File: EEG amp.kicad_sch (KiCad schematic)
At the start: 40 parts, among them J1 Electrodes, J2 Power, J3 Output, J4 Status, U1 AD8232, U2 TMUX154EDGS

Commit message: Messed with schematic and(I think) finished PCB
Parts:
- removed C9: 100nF, Capacitor_SMD:C_0201_0603Metric, symbol Device:C
- removed J2: Power, Connector_PinSocket_2.54mm:PinSocket_1x03_P2.54mm_Vertical, symbol Connector:Conn_01x03_Socket
- removed R11, R12: 33k, Resistor_SMD:R_1206_3216Metric, symbol Device:R_US
- removed R16, R17: 10k ±0.1%, Resistor_SMD:R_0402_1005Metric, symbol Device:R_US
- removed R19, R20, R21: 50R, Resistor_SMD:R_0402_1005Metric, symbol Device:R_US
- removed R9: 150, Resistor_SMD:R_1206_3216Metric, symbol Device:R_US
- removed U2: TMUX154EDGS, Package_SO:VSSOP-10_3x3mm_P0.5mm, symbol Analog_Switch:TMUX154EDGS
- added J2: Power, Connector_PinSocket_2.54mm:PinSocket_1x04_P2.54mm_Vertical, symbol Connector:Conn_01x04_Socket
- added U2: TS5A3159ADBVR, Package_TO_SOT_SMD:SOT-23-6, symbol Analog_Switch:TS5A3159ADBVR
- C1, C2, C8: value 0.1uF -> ECHU1C104GX5; footprint Capacitor_SMD:C_0201_0603Metric -> Capacitor_SMD:C_1210_3225Metric
- C3: value 1nF -> CC0402JRX7R9BB102; footprint Capacitor_SMD:C_0603_1608Metric -> Capacitor_SMD:C_0402_1005Metric
- C4: value 100uF -> CA45-B6R3K107T; footprint Capacitor_SMD:C_0805_2012Metric -> Capacitor_Tantalum_SMD:CP_EIA-3528-21_Kemet-B
- C5, C6: value 10uF -> CA45-A010K106T; footprint Capacitor_SMD:C_0805_2012Metric -> Capacitor_Tantalum_SMD:CP_EIA-3216-12_Kemet-S
- C7: value 14pF -> 0402CG140J500NT; footprint Capacitor_SMD:C_0201_0603Metric -> Capacitor_SMD:C_0402_1005Metric
- D1: value Green -> XL-1608UBC-04; footprint LED_THT:LED_D5.0mm -> LED_SMD:LED_0603_1608Metric
- D2: value Yellow - 2e -> XL-1608UGC-04; footprint LED_THT:LED_D5.0mm -> LED_SMD:LED_0603_1608Metric
- D3: value Yellow - 1e -> XL-1608UGC-04; footprint LED_THT:LED_D5.0mm -> LED_SMD:LED_0603_1608Metric
- D4: value Red -> XL-2012UWC; footprint LED_THT:LED_D5.0mm -> LED_SMD:LED_0805_2012Metric
- R1, R2: value 10k ±0.1% -> ARG03BTC1002; footprint Resistor_SMD:R_0402_1005Metric -> Resistor_SMD:R_0603_1608Metric
- R10: value 33k -> 0603WAD3302T5E; footprint Resistor_SMD:R_1206_3216Metric -> Resistor_SMD:R_0603_1608Metric
- R13: value 1k -> CF1/6W-7.5KΩ±5%T52; footprint Resistor_SMD:R_1206_3216Metric -> Resistor_THT:R_Axial_DIN0207_L6.3mm_D2.5mm_P5.08mm_Vertical
- R14, R15, R18: value 10k -> 1206W4F1002T5E; footprint Resistor_SMD:R_0402_1005Metric -> Resistor_SMD:R_1206_3216Metric
- R3, R5: value 330k -> SCR0402J330K; footprint Resistor_SMD:R_1206_3216Metric -> Resistor_SMD:R_0402_1005Metric
- R4, R8: value 10 -> ARG05DTC1600; footprint Resistor_SMD:R_1206_3216Metric -> Resistor_SMD:R_0805_2012Metric
- R6: value 150 -> 0603WAD3302T5E; footprint Resistor_SMD:R_1206_3216Metric -> Resistor_SMD:R_0603_1608Metric
- R7: value 33k -> 1206W4F1002T5E
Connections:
- net +3.3V: now also C8.1, D1.2 (A), R14.2, J2.2 (Pin_2), U2.5 (V+); no longer D4.2 (A), R14.1
- net 1e: now also U2.3
- net 1o: now also R15.2; no longer R15.1
- net 2e: now also U2.1
- net Aref: now also J2.3 (Pin_3); no longer C8.1
- net GND: now also D4.1 (K), R7.1, J2.4 (Pin_4), U2.2 (GND); no longer D1.1 (K)
- net Ie: now also U2.4
- net OPAMP+1: now also R4.2; no longer R7.2
- net OPAMP-1: now also R13.2, R15.1; no longer R15.2
- net connected1: now also D4.2 (A); no longer D4.1 (K)
- net shutdown: now also D1.1 (K), R14.1; no longer D1.2 (A), R14.2
- net switch: now also R7.2, U2.6
- net at C5.1, C6.2, R10.2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: now also R6.1, R8.2; no longer R7.1
- no-connect marks 3 -> 4
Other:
- moved on the sheet: C7, D1, D4, J3, J4, R13, R18, R8

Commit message: Exported various files for OnBoard
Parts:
- renumbered C4 to C1, C1 to C4, C7 to C5, C5 to C6, C6 to C7, D4 to D1, D1 to D2, D2 to D4, J3 to J2, J2 to J3, R6 to R10, R13 to R11, R7 to R12, R14 to R13, R5 to R2, R10 to R3, R2 to R4, R3 to R5, R8 to R6, R15 to R7, R18 to R8, R4 to R9
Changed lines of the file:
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@@
 		(dnp no)
 		(fields_autoplaced yes)
-		(property "Reference" "C1"
+		(property "Reference" "C4"
 			(at 166.37 21.5899 0)
 			(effects
@@
 			(project "EEG amp"
 				(path "/828fcb53-5b19-4d8c-be04-4f1b7f282370"
-					(reference "C1")
+					(reference "C4")
 					(unit 1)
 				)
@@
 		(on_board yes)
 		(dnp no)
-		(property "Reference" "D2"
+		(property "Reference" "D4"
 			(at 228.9175 85.09 0)
 			(effects
@@
 			(project "EEG amp"
 				(path "/828fcb53-5b19-4d8c-be04-4f1b7f282370"
-					(reference "D2")
+					(reference "D4")
 					(unit 1)
 				)
@@
 		(dnp no)
 		(fields_autoplaced yes)
-		(property "Reference" "D4"
+		(property "Reference" "D1"
 			(at 249.2375 74.93 0)
 			(effects
@@
 			(project "EEG amp"
 				(path "/828fcb53-5b19-4d8c-be04-4f1b7f282370"
-					(reference "D4")
+					(reference "D1")
 					(unit 1)
 				)
@@
 		(dnp no)
 		(fields_autoplaced yes)
-		(property "Reference" "R10"
+		(property "Reference" "R3"
 			(at 153.67 106.68 90)
 			(effects
@@
 			(project "EEG amp"
 				(path "/828fcb53-5b19-4d8c-be04-4f1b7f282370"
-					(reference "R10")
+					(reference "R3")
 					(unit 1)
 				)
@@
 		(dnp no)
 		(fields_autoplaced yes)
-		(property "Reference" "R4"
+		(property "Reference" "R9"
 			(at 184.15 90.17 90)
 			(effects
@@
 			(project "EEG amp"
 				(path "/828fcb53-5b19-4d8c-be04-4f1b7f282370"
-					(reference "R4")
+					(reference "R9")
 					(unit 1)
 				)
@@
 		(dnp no)
 		(fields_autoplaced yes)
-		(property "Reference" "R13"
+		(property "Reference" "R11"
 			(at 151.13 86.3599 0)
 			(effects
@@
 			(project "EEG amp"
 				(path "/828fcb53-5b19-4d8c-be04-4f1b7f282370"
-					(reference "R13")
+					(reference "R11")
 					(unit 1)
 				)
@@
 		(dnp no)
 		(fields_autoplaced yes)
-		(property "Reference" "C6"
+		(property "Reference" "C7"
 			(at 168.91 115.5699 0)
 			(effects
@@
 			(project "EEG amp"
 				(path "/828fcb53-5b19-4d8c-be04-4f1b7f282370"
-					(reference "C6")
+					(reference "C7")
 					(unit 1)
 				)
@@
 		(dnp no)
 		(fields_autoplaced yes)
-		(property "Reference" "R3"
+		(property "Reference" "R5"
 			(at 121.92 16.51 90)
 			(effects
@@
 			(project "EEG amp"
 				(path "/828fcb53-5b19-4d8c-be04-4f1b7f282370"
-					(reference "R3")
+					(reference "R5")
 					(unit 1)
 				)
@@
 		(dnp no)
 		(fields_autoplaced yes)
-		(property "Reference" "C7"
+		(property "Reference" "C5"
 			(at 187.96 146.0499 0)
 			(effects
@@
 			(project "EEG amp"
 				(path "/828fcb53-5b19-4d8c-be04-4f1b7f282370"
-					(reference "C7")
+					(reference "C5")
 					(unit 1)
 				)
@@
 		(dnp no)
 		(fields_autoplaced yes)
-		(property "Reference" "R8"
+		(property "Reference" "R6"
 			(at 153.67 97.79 90)
 			(effects
@@
 			(project "EEG amp"
 				(path "/828fcb53-5b19-4d8c-be04-4f1b7f282370"
-					(reference "R8")
+					(reference "R6")
 					(unit 1)
 				)
@@
 		(dnp no)
 		(fields_autoplaced yes)
-		(property "Reference" "R5"
+		(property "Reference" "R2"
 			(at 115.57 43.18 90)
 			(effects
@@
 			(project "EEG amp"
 				(path "/828fcb53-5b19-4d8c-be04-4f1b7f282370"
-					(reference "R5")
+					(reference "R2")
 					(unit 1)
 				)
@@
 		(dnp no)
 		(fields_autoplaced yes)
-		(property "Reference" "C5"
+		(property "Reference" "C6"
 			(at 168.91 107.9499 0)
 			(effects
@@
 			(project "EEG amp"
 				(path "/828fcb53-5b19-4d8c-be04-4f1b7f282370"
-					(reference "C5")
+					(reference "C6")
 					(unit 1)
 				)
@@
 		(dnp no)
 		(fields_autoplaced yes)
-		(property "Reference" "R6"
+		(property "Reference" "R10"
 			(at 184.15 99.06 90)
 			(effects
@@
 			(project "EEG amp"
 				(path "/828fcb53-5b19-4d8c-be04-4f1b7f282370"
-					(reference "R6")
+					(reference "R10")
 					(unit 1)
 				)
@@
 		(dnp no)
 		(fields_autoplaced yes)
-		(property "Reference" "D1"
+		(property "Reference" "D2"
 			(at 227.6475 72.39 0)
 			(effects
@@
 			(project ""
 				(path "/828fcb53-5b19-4d8c-be04-4f1b7f282370"
-					(reference "D1")
+					(reference "D2")
 					(unit 1)
 				)
@@
 		(dnp no)
 		(fields_autoplaced yes)
-		(property "Reference" "R15"
+		(property "Reference" "R7"
 			(at 160.02 78.7399 0)
 			(effects
@@
 			(project "EEG amp"
 				(path "/828fcb53-5b19-4d8c-be04-4f1b7f282370"
-					(reference "R15")
+					(reference "R7")
 					(unit 1)
 				)
@@
 		(dnp no)
 		(fields_autoplaced yes)
-		(property "Reference" "R2"
+		(property "Reference" "R4"
 			(at 214.63 57.1499 0)
 			(effects
@@
 			(project "EEG amp"
 				(path "/828fcb53-5b19-4d8c-be04-4f1b7f282370"
-					(reference "R2")
+					(reference "R4")
 					(unit 1)
 				)
@@
 		(dnp no)
 		(fields_autoplaced yes)
-		(property "Reference" "C4"
+		(property "Reference" "C1"
 			(at 115.57 52.07 90)
 			(effects
@@
 			(project "EEG amp"
 				(path "/828fcb53-5b19-4d8c-be04-4f1b7f282370"
-					(reference "C4")
+					(reference "C1")
 					(unit 1)
 				)
@@
 		(dnp no)
 		(fields_autoplaced yes)
-		(property "Reference" "R14"
+		(property "Reference" "R13"
 			(at 247.65 35.5599 0)
 			(effects
@@
 			(project "EEG amp"
 				(path "/828fcb53-5b19-4d8c-be04-4f1b7f282370"
-					(reference "R14")
+					(reference "R13")
 					(unit 1)
 				)
@@
 		(dnp no)
 		(fields_autoplaced yes)
-		(property "Reference" "R18"
+		(property "Reference" "R8"
 			(at 194.31 153.67 90)
 			(effects
@@
 			(project "EEG amp"
 				(path "/828fcb53-5b19-4d8c-be04-4f1b7f282370"
-					(reference "R18")
+					(reference "R8")
 					(unit 1)
 				)
@@
 		(dnp no)
 		(fields_autoplaced yes)
-		(property "Reference" "J2"
+		(property "Reference" "J3"
 			(at 274.32 25.3999 0)
 			(effects
@@
 			(project ""
 				(path "/828fcb53-5b19-4d8c-be04-4f1b7f282370"
-					(reference "J2")
+					(reference "J3")
 					(unit 1)
 				)
@@
 		(dnp no)
 		(fields_autoplaced yes)
-		(property "Reference" "J3"
+		(property "Reference" "J2"
 			(at 275.59 86.3599 0)
 			(effects
@@
 			(project ""
 				(path "/828fcb53-5b19-4d8c-be04-4f1b7f282370"
-					(reference "J3")
+					(reference "J2")
 					(unit 1)
 				)
@@
 		(dnp no)
 		(fields_autoplaced yes)
-		(property "Reference" "R7"
+		(property "Reference" "R12"
 			(at 220.98 144.7799 0)
 			(effects
@@
 			(project "EEG amp"
 				(path "/828fcb53-5b19-4d8c-be04-4f1b7f282370"
-					(reference "R7")
+					(reference "R12")
 					(unit 1)
 				)

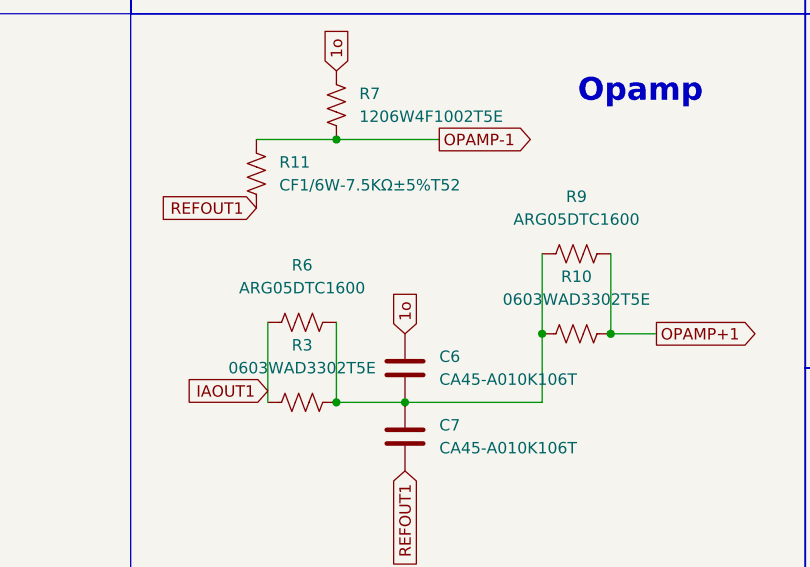
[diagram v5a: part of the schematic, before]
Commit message: adjusted many things, including, apparently, the footprint for one of the resistors
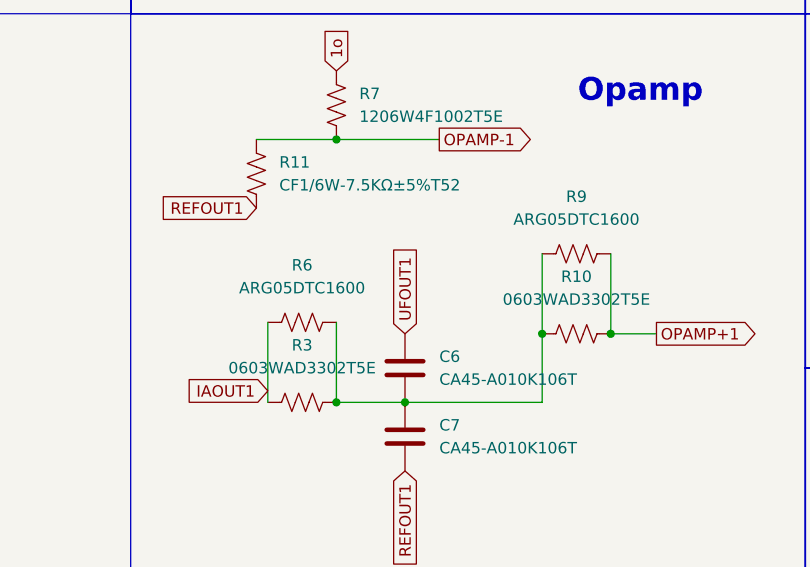
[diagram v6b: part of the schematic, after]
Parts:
- R11: footprint Resistor_THT:R_Axial_DIN0207_L6.3mm_D2.5mm_P5.08mm_Vertical -> Personal:R_Axial_DIN0207_L6.3mm_D2.5mm_P5.08mm_Horizontal
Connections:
- net 1o: no longer C6.2
- net UFOUT1: now also C6.2
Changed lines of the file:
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@@
 		)
 	)
-	(global_label "1o"
-		(shape input)
-		(at 165.1 105.41 90)
+	(global_label "1e"
+		(shape output)
+		(at 266.7 96.52 180)
 		(fields_autoplaced yes)
 		(effects
@@
 				(size 1.27 1.27)
 			)
-			(justify left)
+			(justify right)
 		)
 		(property "Intersheetrefs" "${INTERSHEET_REFS}"
-			(at 165.1 100.0663 90)
-			(effects
-				(font
-					(size 1.27 1.27)
-				)
-				(justify left)
-				(hide yes)
-			)
-		)
-	)
-	(global_label "1e"
-		(shape output)
-		(at 266.7 96.52 180)
+			(at 261.4167 96.52 0)
+			(effects
+				(font
+					(size 1.27 1.27)
+				)
+				(justify right)
+				(hide yes)
+			)
+		)
+	)
+	(global_label "Aref"
+		(shape input)
+		(at 184.15 143.51 90)
 		(fields_autoplaced yes)
 		(effects
@@
 				(size 1.27 1.27)
 			)
-			(justify right)
+			(justify left)
 		)
 		(property "Intersheetrefs" "${INTERSHEET_REFS}"
-			(at 261.4167 96.52 0)
-			(effects
-				(font
-					(size 1.27 1.27)
-				)
-				(justify right)
-				(hide yes)
-			)
-		)
-	)
-	(global_label "Aref"
-		(shape input)
-		(at 184.15 143.51 90)
+			(at 184.15 136.8357 90)
+			(effects
+				(font
+					(size 1.27 1.27)
+				)
+				(justify left)
+				(hide yes)
+			)
+		)
+	)
+	(global_label "Ze"
+		(shape output)
+		(at 266.7 99.06 180)
 		(fields_autoplaced yes)
 		(effects
@@
 				(size 1.27 1.27)
 			)
-			(justify left)
+			(justify right)
 		)
 		(property "Intersheetrefs" "${INTERSHEET_REFS}"
-			(at 184.15 136.8357 90)
-			(effects
-				(font
-					(size 1.27 1.27)
-				)
-				(justify left)
-				(hide yes)
-			)
-		)
-	)
-	(global_label "Ze"
-		(shape output)
-		(at 266.7 99.06 180)
+			(at 261.4167 99.06 0)
+			(effects
+				(font
+					(size 1.27 1.27)
+				)
+				(justify right)
+				(hide yes)
+			)
+		)
+	)
+	(global_label "UFOUT1"
+		(shape input)
+		(at 165.1 105.41 90)
 		(fields_autoplaced yes)
 		(effects
@@
 				(size 1.27 1.27)
 			)
-			(justify right)
+			(justify left)
 		)
 		(property "Intersheetrefs" "${INTERSHEET_REFS}"
-			(at 261.4167 99.06 0)
-			(effects
-				(font
-					(size 1.27 1.27)
-				)
-				(justify right)
+			(at 165.1 95.1676 90)
+			(effects
+				(font
+					(size 1.27 1.27)
+				)
+				(justify left)
 				(hide yes)
 			)
@@
 			)
 		)
-		(property "Footprint" "Resistor_THT:R_Axial_DIN0207_L6.3mm_D2.5mm_P5.08mm_Vertical"
+		(property "Footprint" "Personal:R_Axial_DIN0207_L6.3mm_D2.5mm_P5.08mm_Horizontal"
 			(at 147.574 87.376 90)
 			(effects
